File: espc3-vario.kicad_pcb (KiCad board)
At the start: 2 copper layers, 74 x 34 mm, 54 parts, among them J1 conn_pgm, J2 conn_bat, J3 USB_C_6PIN, Q1 AO3401A, Q2 2N7002, SW1 RST, SW2 PCC, SW3 PWR, U1 CJMCU-117, U2 ESPC3-12F C3FN4, U3 TLV75533PDBV, U4 74HC240PWR, U5 MCP73831-2-OT

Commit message: update
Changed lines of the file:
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@@
-(kicad_pcb (version 20220211) (generator pcbnew)
+(kicad_pcb (version 20220308) (generator pcbnew)
   (general
-    (thickness 1.6)
+    (thickness 1.58)
   )
   (paper "A4")
@@
   (setup
     (stackup
-      (layer "F.SilkS" (type "Top Silk Screen"))
-      (layer "F.Paste" (type "Top Solder Paste"))
-      (layer "F.Mask" (type "Top Solder Mask") (thickness 0.01))
       (layer "F.Cu" (type "copper") (thickness 0.035))
       (layer "dielectric 1" (type "core") (thickness 1.51) (material "FR4") (epsilon_r 4.5) (loss_tangent 0.02))
       (layer "B.Cu" (type "copper") (thickness 0.035))
-      (layer "B.Mask" (type "Bottom Solder Mask") (thickness 0.01))
-      (layer "B.Paste" (type "Bottom Solder Paste"))
-      (layer "B.SilkS" (type "Bottom Silk Screen"))
       (copper_finish "None")
       (dielectric_constraints no)
@@
     (pad_to_mask_clearance 0)
     (aux_axis_origin 90 120)
+    (grid_origin 90 120)
     (pcbplotparams
       (layerselection 0x00010fc_ffffffff)
@@
     (effects (font (size 1 1) (thickness 0.15)) (justify mirror))
   )
+  (target plus (at 90 120) (size 5) (width 0.1) (layer "Edge.Cuts"))
+  (target plus (at 90 120) (size 5) (width 0.1) (layer "Edge.Cuts"))
+  (target plus (at 90 120) (size 5) (width 0.1) (layer "Edge.Cuts"))
   (via (at 138.2 118.15) (size 0.8) (drill 0.4) (layers "F.Cu" "B.Cu") (net 1))
   (segment (start 134.2 116.475) (end 134.2 115.825) (width 0.25) (layer "B.Cu") (net 1))
@@
   (segment (start 117.7 93.95) (end 116.25 92.5) (width 0.4) (layer "F.Cu") (net 26))
   (segment (start 121.01 98.81) (end 117.7 95.5) (width 0.4) (layer "F.Cu") (net 26))
-  (segment (start 109.1 95.3) (end 109.45 95.65) (width 0.4) (layer "F.Cu") (net 27))
-  (segment (start 121.05 100) (end 124.55 100) (width 0.4) (layer "F.Cu") (net 27))
-  (segment (start 109.45 95.65) (end 116.7 95.65) (width 0.4) (layer "F.Cu") (net 27))
-  (segment (start 116.7 95.65) (end 121.05 100) (width 0.4) (layer "F.Cu") (net 27))
+  (segment (start 122.35 101.3) (end 125.85 101.3) (width 0.4) (layer "F.Cu") (net 27))
+  (segment (start 116.7 95.65) (end 122.35 101.3) (width 0.4) (layer "F.Cu") (net 27))
+  (segment (start 125.85 101.3) (end 125.9 101.35) (width 0.4) (layer "F.Cu") (net 27))
   (segment (start 109.1 95.3) (end 109.05 95.25) (width 0.25) (layer "F.Cu") (net 27))
-  (segment (start 124.55 100) (end 125.9 101.35) (width 0.4) (layer "F.Cu") (net 27))
+  (segment (start 109.45 95.65) (end 116.7 95.65) (width 0.4) (layer "F.Cu") (net 27))
   (segment (start 109.05 95.25) (end 109.05 93.95) (width 0.4) (layer "F.Cu") (net 27))
+  (segment (start 109.1 95.3) (end 109.45 95.65) (width 0.4) (layer "F.Cu") (net 27))
   (segment (start 126.89 103.89) (end 127.5 104.5) (width 0.4) (layer "F.Cu") (net 28))
   (segment (start 125.9 103.89) (end 123.44 103.89) (width 0.4) (layer "F.Cu") (net 28))

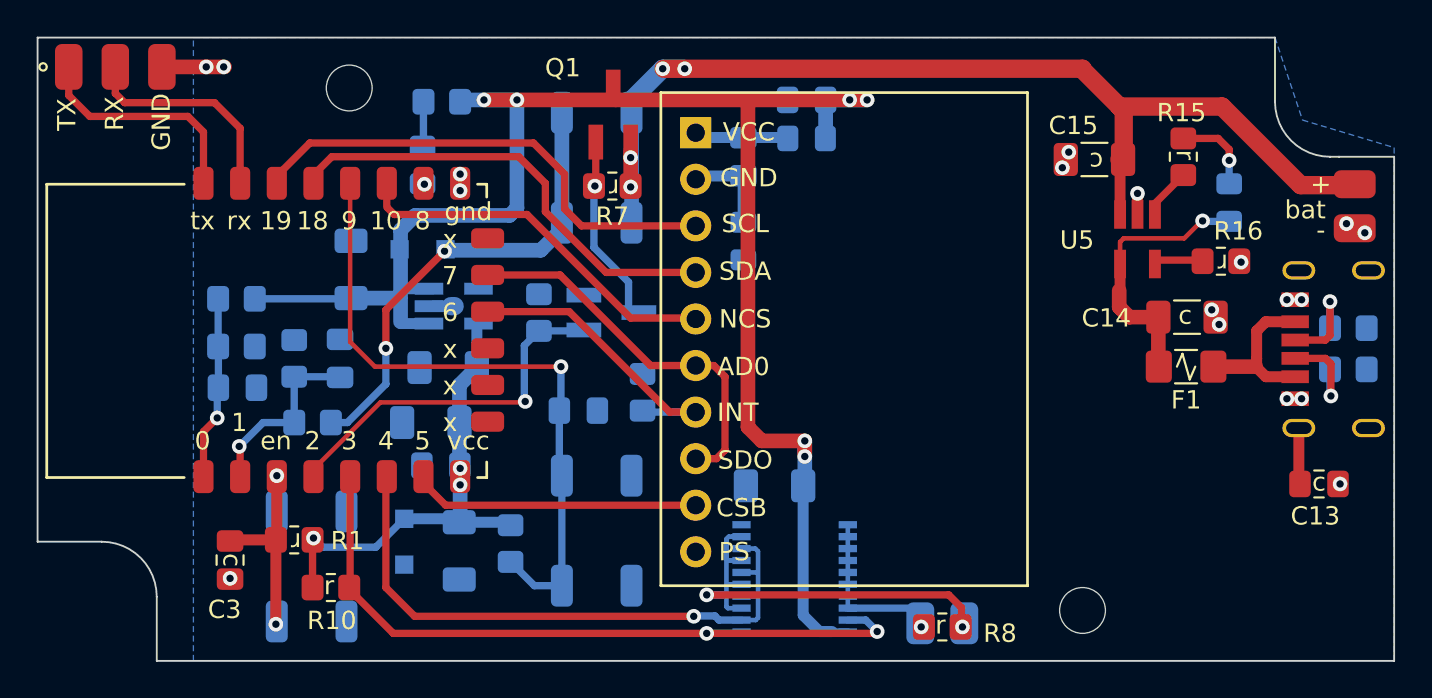
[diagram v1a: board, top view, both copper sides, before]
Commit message: no via in pads, add silkscreen outlines
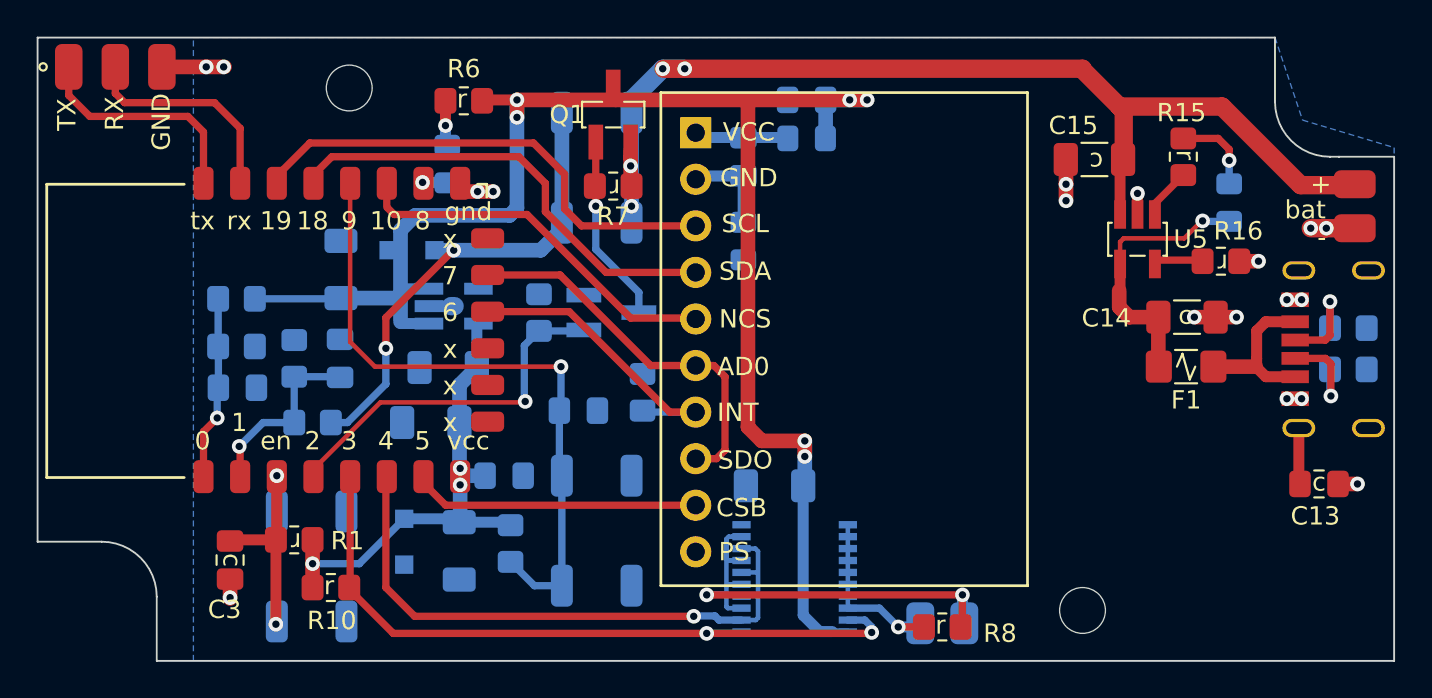
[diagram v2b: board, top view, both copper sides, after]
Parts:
- R6: moved to F.Cu
- moved C10 3.49 mm to (115.5, 109.9), turned to 0 degrees
- moved D2 1.35 mm to (112.3, 92.9)
- moved R6 1.20 mm to (113.2, 89.5)
- moved D1 0.60 mm to (110.4, 97.6)
- moved C9 0.55 mm to (106.5, 98.7)
- moved R7 0.05 mm to (121.4, 94.1)
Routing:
- net GND: track 6.77 -> 19.3 mm
- net +3V3: track 24.2 -> 26.6 mm
- net +VSW: track 92.0 -> 89.9 mm
- net Net-(BZ1-+): track 26.3 -> 28.3 mm
- net Net-(BZ1--): track 8.66 -> 10.1 mm
- net Net-(D2-K): track 0.00 -> 1.40 mm
- net Net-(D1-A): track 25.3 -> 26.1 mm
- net Net-(D2-A): track 2.45 -> 2.37 mm, vias 0 -> 1
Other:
- board text removed: "U3"
